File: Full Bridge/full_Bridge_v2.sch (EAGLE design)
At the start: 28 parts, among them Q1 IRF520, Q4 IRF520, Q5 IRF520, Q8 IRF520

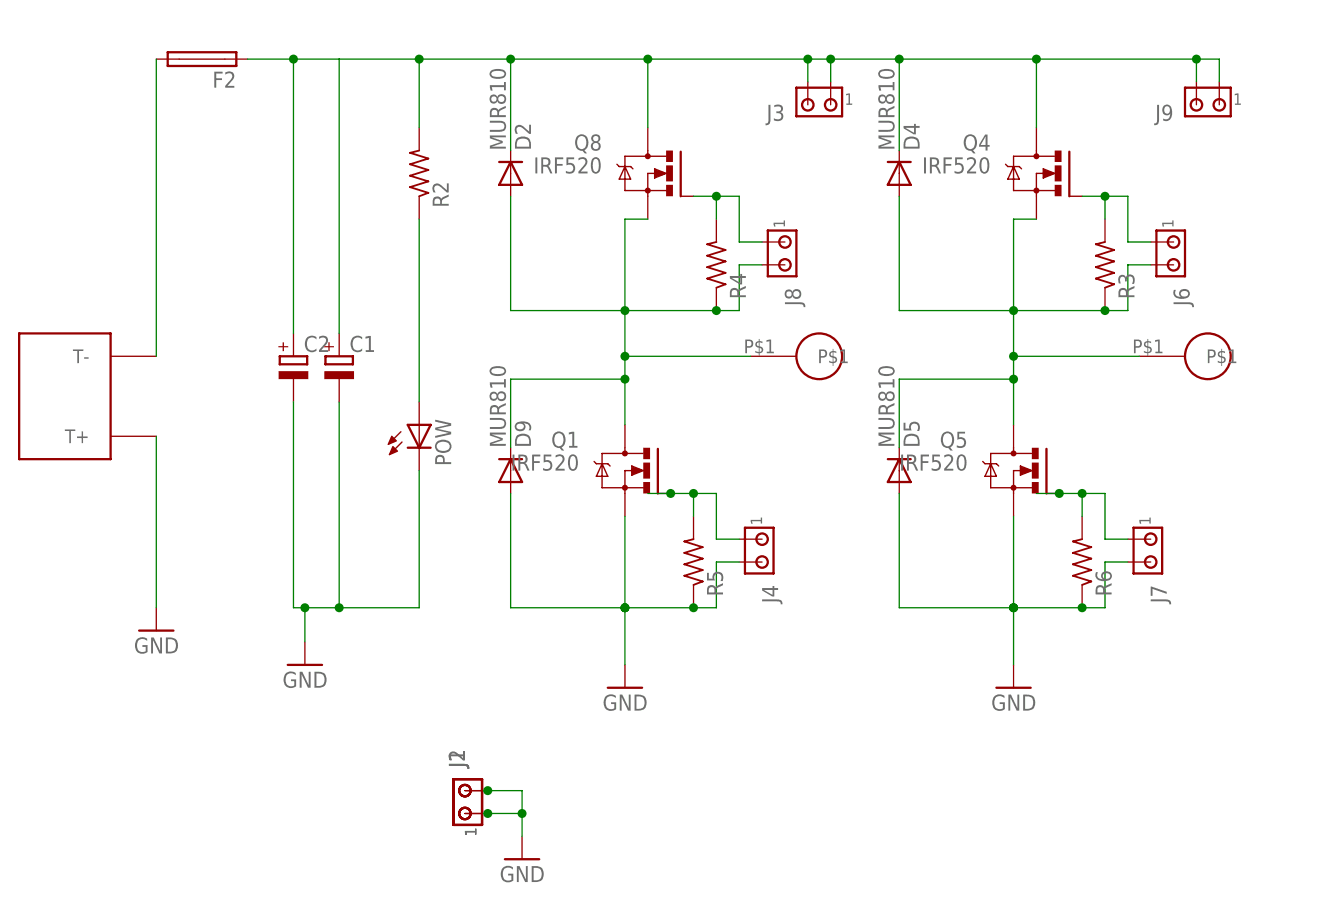
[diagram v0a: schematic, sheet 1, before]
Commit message: h-bridge components value updated
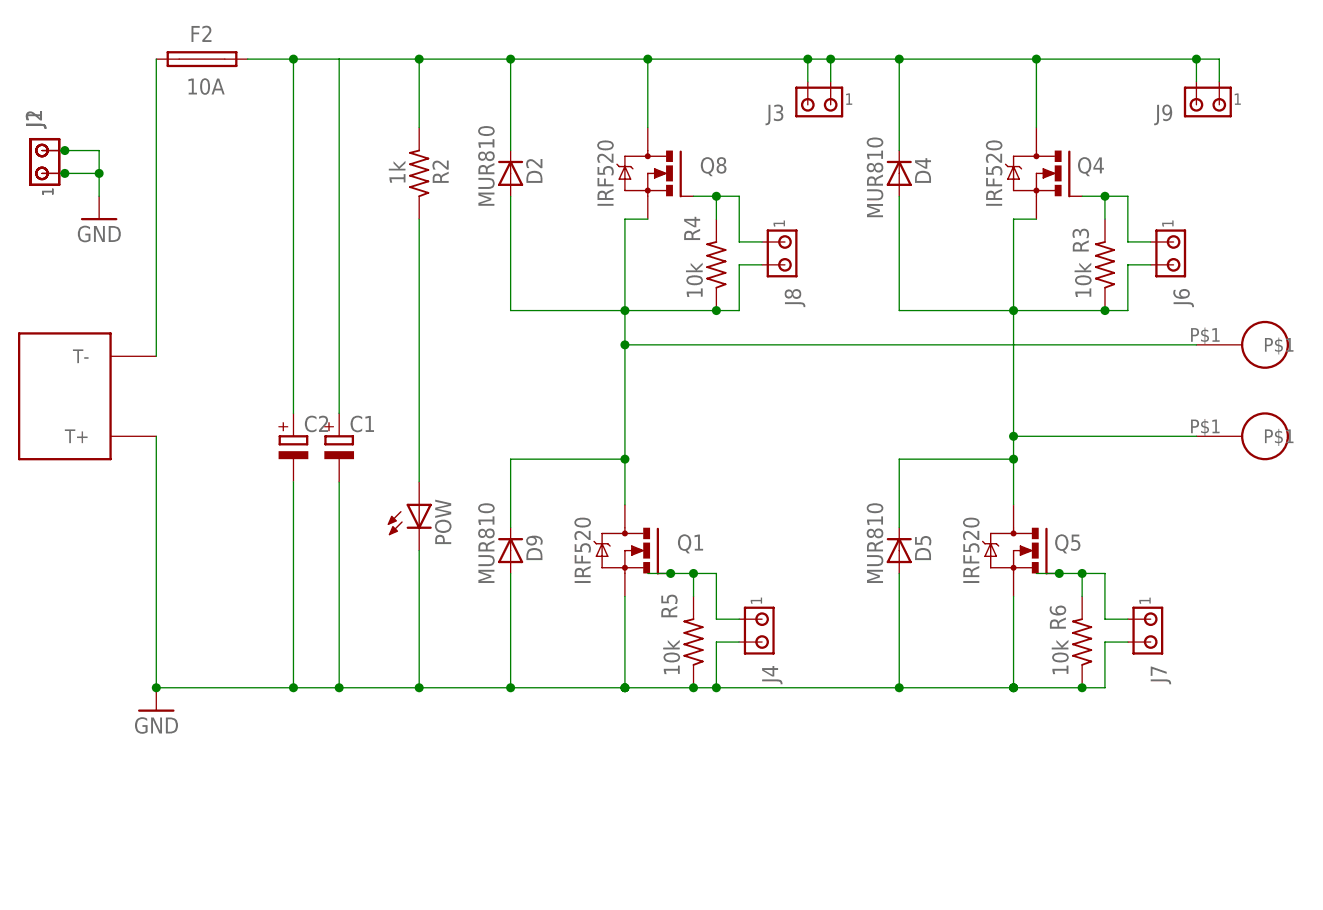
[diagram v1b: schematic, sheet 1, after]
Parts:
- removed U$3, U$4: TERMINAL, terminal:TERMINAL
- added AC1, AC2: TERMINAL, terminal:TERMINAL
- F2: value (none) -> 10A
- R2: value (none) -> 1k
- R3, R4, R5, R6: value (none) -> 10k
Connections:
- net HVDC renamed DC_BUS
- net A_MID: now also AC1.P$1; no longer U$3.P$1
- net A_MID1: now also AC2.P$1; no longer U$4.P$1
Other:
- moved on the sheet: C1, C2, D5, D9, J1, J2, J4, J7, POW, Q1, Q5, R5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
